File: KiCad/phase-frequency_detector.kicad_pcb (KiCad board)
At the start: 2 copper layers, 160 x 100 mm, 89 parts, among them J1 REF, J2 IN, J3 Error_Out, J4 C64AC, J5 Switch, J6 Fast_Out, U1 HMC439QS16G, U2 LT3045EMSE, U3 LT3094EMSE, U4 ADA4896-2ARMZ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

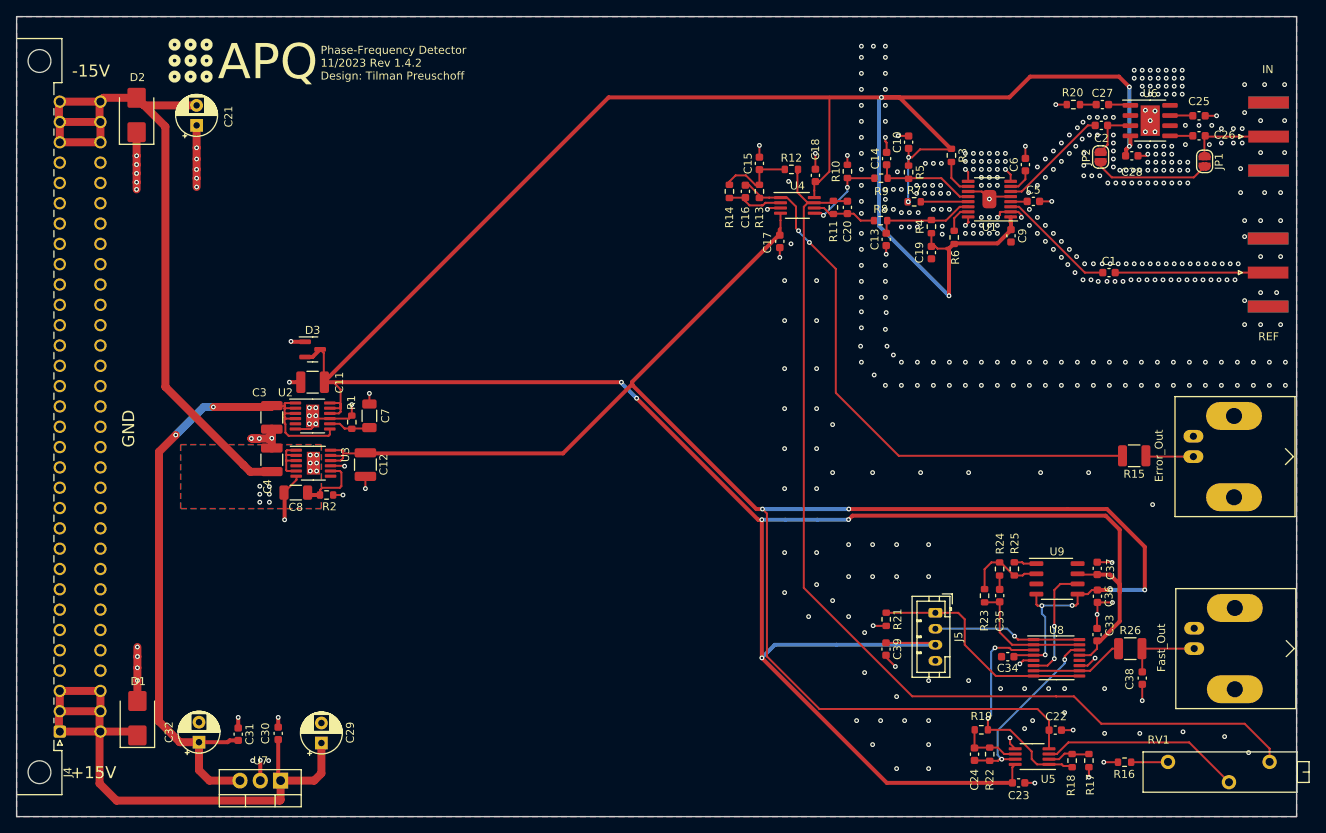
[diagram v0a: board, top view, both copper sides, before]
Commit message: Move BNC connectors to be flush with edge-mount SMA connectors
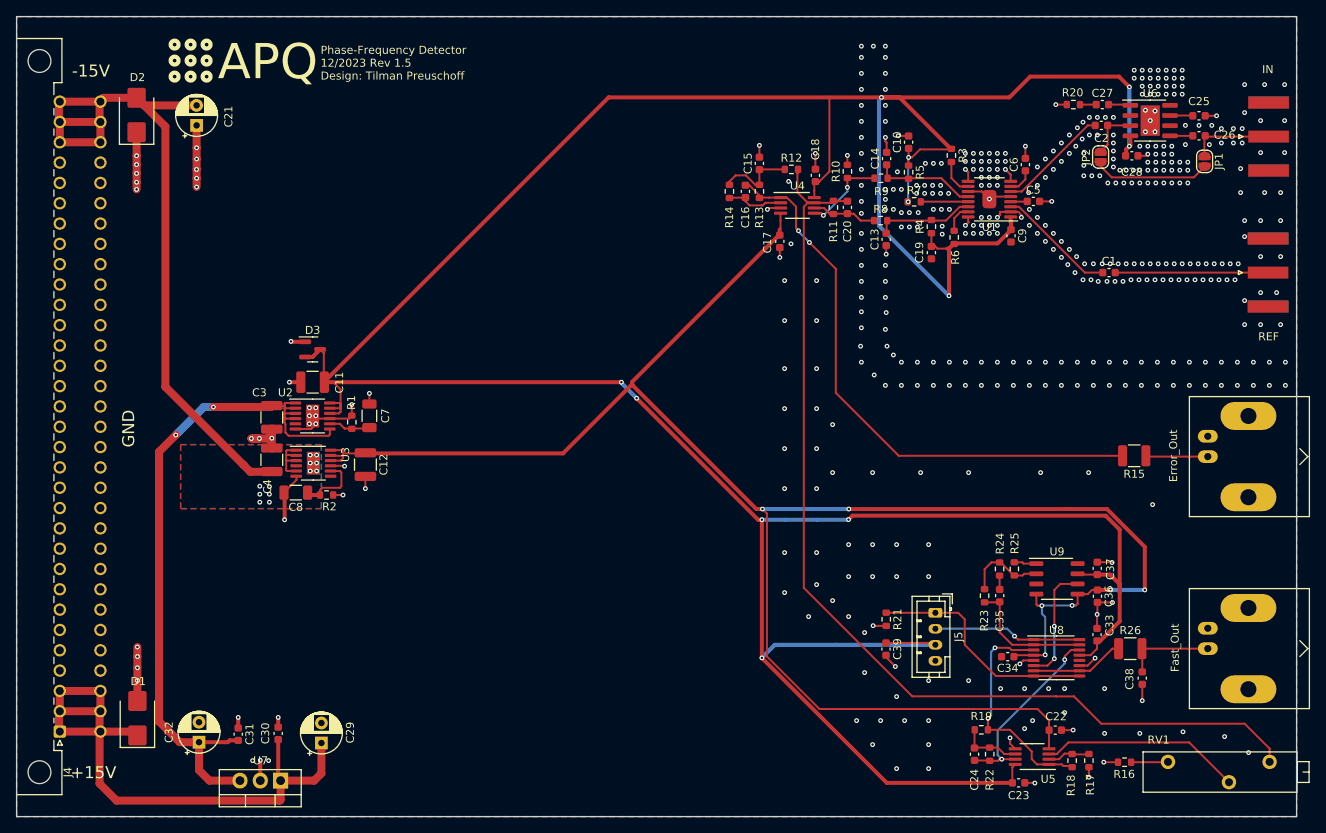
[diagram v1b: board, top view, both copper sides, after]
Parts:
- moved J3 1.80 mm to (218.9, 105.0)
- moved J6 1.70 mm to (218.9, 129.0)
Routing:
- net Net-(J6-In): track 9.46 -> 11.2 mm
- net Net-(J3-In): track 6.24 -> 7.84 mm
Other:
- board text added: "Phase-Frequency Detector 12/2023 Rev 1.5 Design: Tilman Preuschoff"
- board text removed: "Phase-Frequency Detector 11/2023 Rev 1.4.2 Design: Tilman Preuschoff"
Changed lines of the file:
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@@
   (title_block
     (title "Phase-Frequency Detector")
-    (date "2023-06-16")
-    (rev "1.4.2")
+    (date "2023-12-15")
+    (rev "1.5")
     (company "Atoms Photons Quanta, Institut für Angewandte Physik, TU Darmstadt")
     (comment 1 "Tilman Preuschoff")
@@
   )
   (footprint "Connector_Coaxial:BNC_Amphenol_B6252HB-NPP3G-50_Horizontal" locked (layer "F.Cu")
-    (at 217.1 105 -90)
+    (at 218.9 105 -90)
     (descr "http://www.farnell.com/datasheets/612848.pdf")
     (tags "BNC Amphenol Horizontal")
@@
   )
   (footprint "Connector_Coaxial:BNC_Amphenol_B6252HB-NPP3G-50_Horizontal" locked (layer "F.Cu")
-    (at 217.2 129 -90)
+    (at 218.9 129 -90)
     (descr "http://www.farnell.com/datasheets/612848.pdf")
     (tags "BNC Amphenol Horizontal")
@@
   (gr_line (start 230 150) (end 230 50)
     (stroke (width 0.15) (type solid)) (layer "Edge.Cuts"))
-  (gr_text "Phase-Frequency Detector\n11/2023 Rev 1.4.2\nDesign: Tilman Preuschoff" (at 108 55.8) (layer "F.SilkS")
+  (gr_text "Phase-Frequency Detector\n12/2023 Rev 1.5\nDesign: Tilman Preuschoff" (at 108 55.8) (layer "F.SilkS")
     (effects (font (size 1 1) (thickness 0.2)) (justify left))
   )
@@
   (segment (start 206.5 61) (end 209.13 61) (width 0.25) (layer "F.Cu") (net 22))
   (segment (start 209.28375 143.2) (end 213.91625 143.2) (width 0.25) (layer "F.Cu") (net 23))
-  (segment (start 217.1934 129.0066) (end 217.2 129) (width 0.25) (layer "F.Cu") (net 24))
   (segment (start 210.7057 131.9146) (end 210.7057 129.0427) (width 0.25) (layer "F.Cu") (net 24))
+  (segment (start 210.6696 129.0066) (end 218.8934 129.0066) (width 0.25) (layer "F.Cu") (net 24))
   (segment (start 210.7057 129.0427) (end 210.6696 129.0066) (width 0.25) (layer "F.Cu") (net 24))
-  (segment (start 210.6696 129.0066) (end 217.1934 129.0066) (width 0.25) (layer "F.Cu") (net 24))
+  (segment (start 218.8934 129.0066) (end 218.9 129) (width 0.25) (layer "F.Cu") (net 24))
   (segment (start 206.375 66.025) (end 205.5 66.9) (width 0.25) (layer "F.Cu") (net 25))
   (segment (start 206.375 63.6) (end 206.375 66.025) (width 0.25) (layer "F.Cu") (net 25))
@@
   (segment (start 201.0156 130.8481) (end 201.0156 130.3782) (width 0.25) (layer "B.Cu") (net 30))
   (segment (start 193.1419 142.8239) (end 192.621991 142.303991) (width 0.25) (layer "B.Cu") (net 30))
-  (segment (start 217.3 105) (end 211.2 105) (width 0.25) (layer "F.Cu") (net 31))
+  (segment (start 218.9 105) (end 211.2 105) (width 0.25) (layer "F.Cu") (net 31))
   (segment (start 211.2 105) (end 211.1 104.9) (width 0.25) (layer "F.Cu") (net 31))
   (segment (start 192.8749 119.8748) (end 192.8749 121.5895) (width 0.25) (layer "F.Cu") (net 32))
